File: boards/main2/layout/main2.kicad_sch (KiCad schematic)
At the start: 218 parts, among them IC1 STM32H725RGV6, IC2 LSM6DSVTR, IC6 STSPIN958TR, IC7 L6981C33DR, IC8 DRV8874PWPR, IC9 DRV8874PWPR, J1 B02B-PASK(LF)(SN), M1 B02B-PASK(LF)(SN), M2 B02B-PASK(LF)(SN), M3 B02B-PASK(LF)(SN), Q1 AO3400A, Q2 AO3400A, Q3 AO3400A, Q4 AO3400A, Q5 AO3400A, Q6 HSBB3072, Q8 AO3401A, Q9 AO3400A, SW1 DSHP04TJGER, SW2 GT-TC048B-H025-L1, SW3 GT-TC048B-H025-L1, SW4 MK-12D18-G040, SW5 GT-TC048B-H025-L1, U10 INA241A2IDGKR, U11 INA241A2IDGKR, U12 TLV9001IDBVR, U13 ESP32-S3-MINI-1-N8, U2 GT-USB-7010ASV, U6 USBLC6-2SC6, U8 ADP7142ACPZN3.3-R7, U9 INA228AIDGSR

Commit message: ✨ Give each main2 module its own schematic sheet
As on the main board: each module declares Project(..., layout=False), its signal ports take the
names of the nets they carry, GND_BAT is a ground port of REGULATORS, and erc.toml accepts the
two ERC warnings pcb 0.4.81's labels leave (diodeinc/pcb#1520). The netlist is unchanged (174
nets, same connectivity). The root's SENSORS pin labels run past the page's left edge until a pcb
release includes diodeinc/pcb#1522; tests/test_schematic.py expects it.
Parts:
- removed BZ1: FUET-5030, Team-Micras_MicrasPCB_components_fuet_FUET-5030:BUZ-SMD_FST-5030, symbol FUET-5030
- removed C100, C103, C106, C108, C18, C19, C20, C21, C24, C25, C32, C55, C59, C60, C70, C72, C79, C82, C88, C90, C91, C97: 100nF 10% 50V X7R, stdlib_kicad-footprints_Capacitor_SMD:C_0402_1005Metric, symbol C_Small
- removed C101, C104, C30: 10nF 10% 50V X7R, stdlib_kicad-footprints_Capacitor_SMD:C_0402_1005Metric, symbol C_Small
- removed C102, C105: 1nF 5% 50V C0G, stdlib_kicad-footprints_Capacitor_SMD:C_0402_1005Metric, symbol C_Small
- removed C107, C52, C63, C80, C81: 10uF 20% 25V X5R, stdlib_kicad-footprints_Capacitor_SMD:C_0603_1608Metric, symbol C_Small
- removed C109, C56, C57: 22uF 20% 25V X5R, stdlib_kicad-footprints_Capacitor_SMD:C_0805_2012Metric, symbol C_Small
- removed C110, C26, C27, C28, C29, C33, C53, C54, C69, C71: 1uF 10% 25V X5R, stdlib_kicad-footprints_Capacitor_SMD:C_0402_1005Metric, symbol C_Small
- removed C31: 220nF 10% 16V X7R, stdlib_kicad-footprints_Capacitor_SMD:C_0402_1005Metric, symbol C_Small
- removed C34, C35: 470nF 10% 50V X7R, stdlib_kicad-footprints_Capacitor_SMD:C_0603_1608Metric, symbol C_Small
- removed C36, C83, C84, C85, C86, C92, C93, C94, C95, C99: 10uF 10% 50V X7R, stdlib_kicad-footprints_Capacitor_SMD:C_1206_3216Metric, symbol C_Small
- removed C58: 47nF 10% 50V X7R, stdlib_kicad-footprints_Capacitor_SMD:C_0603_1608Metric, symbol C_Small
- removed C87, C96: 100uF 20% 25V, Team-Micras_MicrasPCB_components_jierr_JVS25V100M6X4:CAP-SMD_BD6.3-L6.6-W6.6-LS7.3-FD_JVS25V100M6X4, symbol JVS25V100M6X4
- removed C89, C98: 22nF 10% 50V X7R, stdlib_kicad-footprints_Capacitor_SMD:C_0402_1005Metric, symbol C_Small
- removed D1, D2: WS2812C-2020-V6, Team-Micras_MicrasPCB_components_worldsemi_WS2812C-2020:LED-SMD_4P-L2.2-W2.0-P1.00_WS2812C-2020-V6, symbol WS2812C-2020-V6
- removed D14: B5819W, Team-Micras_MicrasPCB_components_cj_B5819W:D_SOD-123, symbol B5819W
- removed D3: 1N4148W, Team-Micras_MicrasPCB_components_hongjiacheng_1N4148W:SOD-123_L2.7-W1.6-LS3.7-FD, symbol 1N4148W
- removed D4: LED YELLOW, stdlib_kicad-footprints_LED_SMD:LED_0603_1608Metric, symbol LED_Small_Filled_Yellow
- removed D5: LED RED, stdlib_kicad-footprints_LED_SMD:LED_0603_1608Metric, symbol LED_Small_Filled_Red
- removed D8: 5V TVS Diode, stdlib_kicad-footprints_Diode_SMD:D_SOD-882, symbol D_TVS_Small
- removed EC1, EC2: EncoderSlot, Team-Micras_MicrasPCB_components_micras_EncoderSlot:EncoderSlot_2x4_P0.95mm, symbol EncoderSlot
- removed ESP_BOOT1, ESP_EN1: TestPoint, Team-Micras_MicrasPCB_components_micras_TestPoint:TestPoint_Pad_D0.8mm, symbol TestPoint
- removed IC2: LSM6DSVTR, Team-Micras_MicrasPCB_components_st_LSM6DSV:LGA-14_3x2.5mm_P0.5mm, symbol LSM6DSV
- removed IC6: STSPIN958TR, Team-Micras_MicrasPCB_components_st_STSPIN958:QFN50P500X500X100-33N-D, symbol STSPIN958
- removed IC7: L6981C33DR, Team-Micras_MicrasPCB_components_st_L6981:SOIC127P600X175-8N, symbol L6981C33DR
- removed IC8, IC9: DRV8874PWPR, Team-Micras_MicrasPCB_components_ti_DRV8874:Texas_PWP0016J_HTSSOP-16-1EP_4.4x5mm_P0.65mm_EP3.4x5mm_Mask2.46x3.55mm, symbol DRV8874PWPR
- removed J1, M1, M2, M3: B02B-PASK(LF)(SN), Team-Micras_MicrasPCB_components_jst_B02B-PASK:JST_PA_B02B-PASK_1x02_P2.00mm_Vertical, symbol B02B-PASK
- removed L3: 22uH 20% 2.8A, Team-Micras_MicrasPCB_components_yjycoin_YSPIA0645-220M:IND-SMD_L6.5-W6.0, symbol YSPIA0645-220M
- removed L4, L5: 47uH 20% 4.1A, Team-Micras_MicrasPCB_components_coilcraft_XAL7070-473:L_Coilcraft_XAL7070-XXX, symbol XAL7070-473MEC
- removed L6: 4.7uH 20% 6.7A, Team-Micras_MicrasPCB_components_coilcraft_XGL5030-472:L_Coilcraft_XAL5030-XXX, symbol XGL5030-472MEC
- removed Q1, Q2, Q3, Q4, Q5, Q9: AO3400A, Team-Micras_MicrasPCB_components_aos_AO3400A:SOT-23-3_L2.9-W1.3-P1.90-LS2.4-BR, symbol AO3400A
- removed Q6: HSBB3072, Team-Micras_MicrasPCB_components_huashuo_HSBB3072:PRPAK-8_L3.0-W3.0-P0.65-BL-EP, symbol HSBB3072
- removed Q8: AO3401A, Team-Micras_MicrasPCB_components_aos_AO3401A:SOT-23, symbol AO3401A
- removed R1, R11, R15, R19, R23: 220 1%, stdlib_kicad-footprints_Resistor_SMD:R_0402_1005Metric, symbol R_Small
- removed R12, R16, R2, R20, R24, R42, R56, R60, R68, R69, R70, R80, R89, R90: 10k 1%, stdlib_kicad-footprints_Resistor_SMD:R_0402_1005Metric, symbol R_Small
- removed R13, R17, R21, R25: 3.3 1% 100mW, stdlib_kicad-footprints_Resistor_SMD:R_0603_1608Metric, symbol R_Small
- removed R14, R18, R22, R26, R30, R87: 1k 1%, stdlib_kicad-footprints_Resistor_SMD:R_0402_1005Metric, symbol R_Small
- removed R27: 39k 1%, stdlib_kicad-footprints_Resistor_SMD:R_0402_1005Metric, symbol R_Small
- removed R28, R91: 22k 1%, stdlib_kicad-footprints_Resistor_SMD:R_0402_1005Metric, symbol R_Small
- removed R29: 9.1k 1%, stdlib_kicad-footprints_Resistor_SMD:R_0402_1005Metric, symbol R_Small
- removed R3: 10 1% 250mW, stdlib_kicad-footprints_Resistor_SMD:R_1206_3216Metric, symbol R_Small
- removed R31: 25m 1% 1W, stdlib_kicad-footprints_Resistor_SMD:R_1206_3216Metric, symbol R_Small
- removed R4, R5, R81: 680 1%, stdlib_kicad-footprints_Resistor_SMD:R_0402_1005Metric, symbol R_Small
- removed R41, R43, R44, R49: 100k 1%, stdlib_kicad-footprints_Resistor_SMD:R_0402_1005Metric, symbol R_Small
- removed R45: 20k 1%, stdlib_kicad-footprints_Resistor_SMD:R_0402_1005Metric, symbol R_Small
- removed R47, R92: 33k 1%, stdlib_kicad-footprints_Resistor_SMD:R_0402_1005Metric, symbol R_Small
- removed R48: 82k 1%, stdlib_kicad-footprints_Resistor_SMD:R_0402_1005Metric, symbol R_Small
- removed R57: 1M 1%, stdlib_kicad-footprints_Resistor_SMD:R_0402_1005Metric, symbol R_Small
- removed R58, R84, R85, R86: 22 1%, stdlib_kicad-footprints_Resistor_SMD:R_0402_1005Metric, symbol R_Small
- removed R59: 2m 1% 1W, Team-Micras_MicrasPCB_components_vishay_WSK2512-MID:Vishay_WSK2512_6332Metric_1mR-4m9R, symbol WSK2512-MID
- removed R6, R7: 5.1k 1%, stdlib_kicad-footprints_Resistor_SMD:R_0402_1005Metric, symbol R_Small
- removed R61, R71: 2k 1%, stdlib_kicad-footprints_Resistor_SMD:R_0402_1005Metric, symbol R_Small
- removed R62, R72: 0, stdlib_kicad-footprints_Resistor_SMD:R_0402_1005Metric, symbol R_Small
- removed R63, R73: 5.6k 1%, stdlib_kicad-footprints_Resistor_SMD:R_0402_1005Metric, symbol R_Small
- removed R64, R74: 24k 1%, stdlib_kicad-footprints_Resistor_SMD:R_0402_1005Metric, symbol R_Small
- removed R65, R75: 10m 1% 1W, Team-Micras_MicrasPCB_components_vishay_WSK2512-HIGH:Vishay_WSK2512_6332Metric_5mR-200mR, symbol WSK2512-HIGH
- removed R66, R76, R77: 0 1W, stdlib_kicad-footprints_Resistor_SMD:R_2512_6332Metric, symbol R_Small
- removed R78, R79, R82, R88: 100 1%, stdlib_kicad-footprints_Resistor_SMD:R_0402_1005Metric, symbol R_Small
- removed R83: 1.2 0.1% 100mW, stdlib_kicad-footprints_Resistor_SMD:R_0603_1608Metric, symbol R_Small
- removed SW1: DSHP04TJGER, Team-Micras_MicrasPCB_components_kangshen_DSHP04TJGER:SW-SMD_8P-L6.7-W5.4-P1.27-LS5.6, symbol DSHP04TJGER
- removed SW2, SW3, SW5: GT-TC048B-H025-L1, Team-Micras_MicrasPCB_components_g-switch_GT-TC048B-H025-L1:SW-SMD-4P_L4.2-W3.2_GT-TC048, symbol GT-TC048B-H025-L1
- removed SW4: MK-12D18-G040, Team-Micras_MicrasPCB_components_g-switch_MK-12D18-G040:SW-TH_MK-12D18-G040, symbol MK-12D18-G040
- removed U10, U11: INA241A2IDGKR, Team-Micras_MicrasPCB_components_ti_INA241A2:Texas_DGK0008A_VSSOP-8_3x3mm_P0.65mm, symbol INA241A2
- removed U12: TLV9001IDBVR, Team-Micras_MicrasPCB_components_ti_TLV9001:SOT-23-5, symbol TLV9001IDBVR
- removed U13: ESP32-S3-MINI-1-N8, Team-Micras_MicrasPCB_components_espressif_ESP32-S3-MINI-1:ESP32-S3-MINI-1, symbol ESP32-S3-MINI-1
- removed U2: GT-USB-7010ASV, Team-Micras_MicrasPCB_components_g-switch_GT-USB-7010ASV:USB-C_G-Switch_GT-USB-7010ASV, symbol GT-USB-7010ASV
- removed U6: USBLC6-2SC6, Team-Micras_MicrasPCB_components_st_USBLC6-2SC6:SOT-23-6_ST_USBLC6-2SC6, symbol USBLC6-2SC6
- removed U8: ADP7142ACPZN3.3-R7, Team-Micras_MicrasPCB_components_adi_ADP7142:LFCSP-6-1EP_2x2mm_P0.65mm_EP1x1.6mm, symbol ADP7142ACPZN3.3-R7
- removed U9: INA228AIDGSR, Team-Micras_MicrasPCB_components_ti_INA228:Texas_DGS0010A_VSSOP-10_3x3mm_P0.5mm, symbol INA228
- removed W1, W2, W3, W4: WallSensor, Team-Micras_MicrasPCB_components_micras_WallSensor:WallSensor_SFH4550_TPS601A_THT, symbol WallSensor
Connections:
- no-connect marks 35 -> 0
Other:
- added sheet DRIVERS (DRIVERS.kicad_sch)
- added sheet ESP (ESP.kicad_sch)
- added sheet PERIPHERALS (PERIPHERALS.kicad_sch)
- added sheet REGULATORS (REGULATORS.kicad_sch)
- added sheet SENSORS (SENSORS.kicad_sch)
- moved on the sheet: C1, C10, C11, C12, C13, C14, C15, C16, C17, C2, C3, C4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

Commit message: 🐛 Keep main2's root labels on the page
SENSORS took three Spi ports, one per device, so the shared SCK, MISO and MOSI came in three times: 32 sheet pins. pcb 0.4.81 places the root's sheet symbols one by one in the order of their names, each as near the page centre as the earlier ones leave room and by its box alone, and a 32-pin SENSORS fitted only against the page's left edge, where the labels at its pins ran up to 11 mm past the page.

SENSORS now takes the bus once (SPI_SCK, SPI_MISO, SPI_MOSI) and each device's chip select (IMU_SPI_CSn, Encoder_Right_CSn, Encoder_Left_CSn), and builds the three Spi interfaces inside. With 26 pins it sits right of ESP, and every label is on its page, so the strict xfail in tests/test_schematic.py goes. The ports take their nets' names, which leaves 8 multiple_net_names warnings instead of 14. The netlist is unchanged: the same 174 nets with the same names and pins.
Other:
- sheet SENSORS ports: added Encoder_Left_CSn, Encoder_Right_CSn, IMU_SPI_CSn, SPI_MISO, SPI_MOSI, SPI_SCK; removed ENCODER_LEFT_SPI.CLK, ENCODER_LEFT_SPI.CS, ENCODER_LEFT_SPI.MISO, ENCODER_LEFT_SPI.MOSI, ENCODER_RIGHT_SPI.CLK, ENCODER_RIGHT_SPI.CS, ENCODER_RIGHT_SPI.MISO, ENCODER_RIGHT_SPI.MOSI, IMU_SPI.CLK, IMU_SPI.CS, IMU_SPI.MISO, IMU_SPI.MOSI
- moved on the sheet: C1, C10, C11, C12, C13, C14, C15, C16, C17, C2, C3, C4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

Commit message: 🎨 Place main2's root sheet: the MCU with its supply domains, and the module sheets
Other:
- note added: "M2 screw holes to the chassis"
- note added: "MCU: STM32H725RGV6, its supply domains and their decoupling"
- note added: "Module sheets: power, radio, user interface"
- note added: "Module sheets: sensors, drivers"
- note added: "Test pads: IMU interrupts and fan driver (bare pads)"
- note added: "Test pads: SWD backstop (bare pads)"
- title: (none) -> MCU and module sheets
- moved on the sheet: C1, C10, C11, C12, C13, C14, C15, C16, C17, C2, C3, C4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

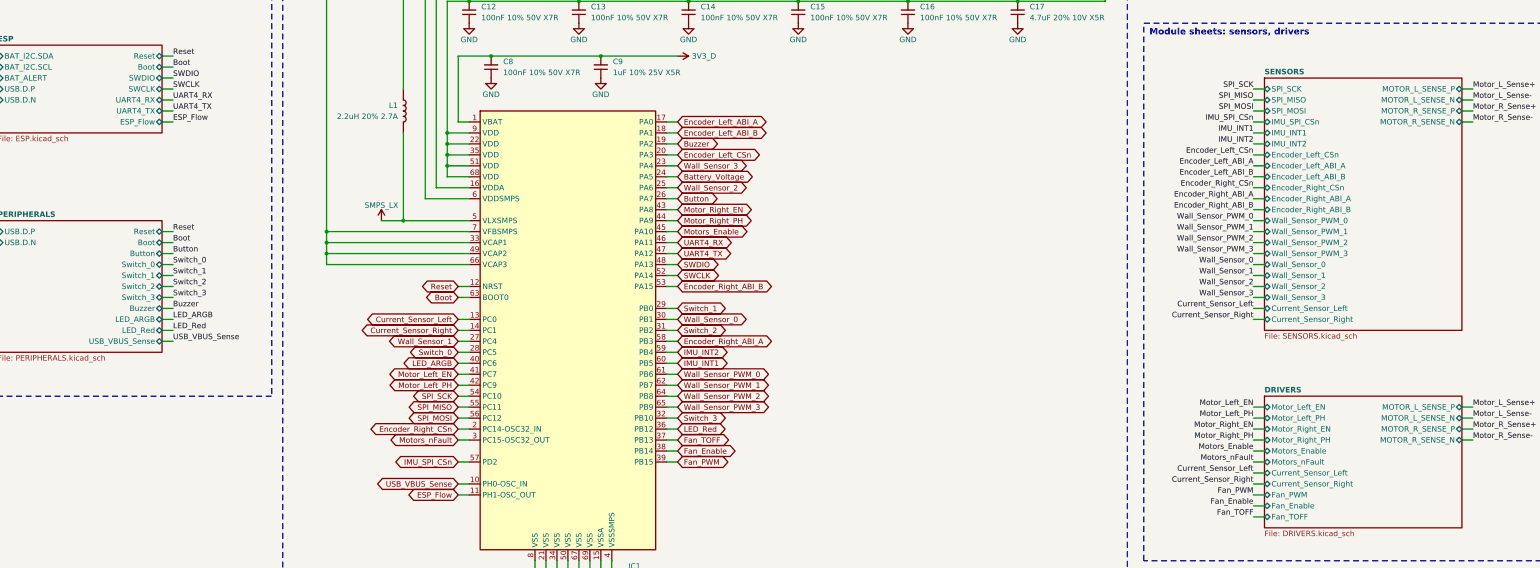
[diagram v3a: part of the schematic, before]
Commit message: ✨ Set main2's emitter current from the DAC and AC-couple its selectors
- The shared sink's set-point comes from PA5 (DAC1_OUT2, buffer off) through
  200k/20k, ratiometric to VDDA and 0 V at reset; 1k/1 nF compensates the loop
  into Q9 and 200k from 3V3_A turns the sink off at a zero set-point.
- Q2-Q5 keep the main board's AC-coupled gates (220 nF, 22k, 1N4148WS clamp):
  a pin held high turns its emitter off within 11 ms.
- Battery_Voltage moves to PC5, Switch_0 to PH0; the H7's VBUS divider goes,
  the ESP32 reports USB power over UART4.
- A test bench checks the selector coupling and the DAC set-point; the
  research model is calculations/emitter/emitter_sink.py.
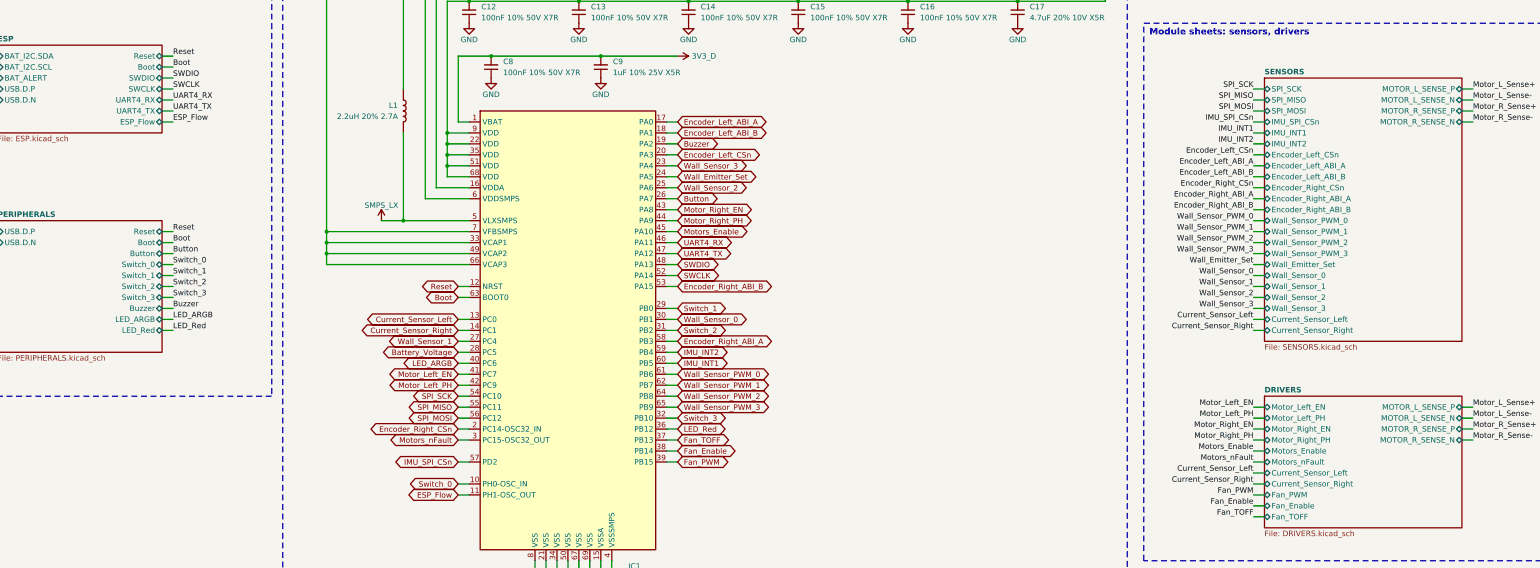
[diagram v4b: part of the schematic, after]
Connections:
- net USB_VBUS_Sense is gone; now on net Switch_0: IC1.10 (PH0-OSC_IN)
- net Battery_Voltage: now also IC1.28 (PC5); no longer IC1.24 (PA5)
- net Switch_0: no longer IC1.28 (PC5)
- new net Wall_Emitter_Set: IC1.24 (PA5)
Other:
- sheet PERIPHERALS ports: added none; removed USB_VBUS_Sense
- sheet SENSORS ports: added Wall_Emitter_Set; removed none
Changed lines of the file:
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@@
 			)
 		)
-		(pin "USB_VBUS_Sense" bidirectional
-			(at 83.82 144.78 0)
-			(effects
-				(font
-					(size 1.27 1.27)
-				)
-				(justify right)
-			)
-		)
 		(instances
 			(project "main2"
@@
 	(sheet
 		(at 339.09 83.82)
-		(size 45.72 58.42)
+		(size 45.72 60.96)
 		(exclude_from_sim no)
 		(in_bom yes)
@@
 		)
 		(property "Sheetfile" "SENSORS.kicad_sch"
-			(at 339.09 142.8338 0)
+			(at 339.09 145.3738 0)
 			(show_name no)
 			(do_not_autoplace no)
@@
 		)
 		(pin "Current_Sensor_Left" bidirectional
-			(at 339.09 137.16 180)
+			(at 339.09 139.7 180)
 			(effects
 				(font
@@
 		)
 		(pin "Current_Sensor_Right" bidirectional
-			(at 339.09 139.7 180)
+			(at 339.09 142.24 180)
 			(effects
 				(font
@@
 			)
 		)
-		(pin "Wall_Sensor_0" bidirectional
+		(pin "Wall_Emitter_Set" bidirectional
 			(at 339.09 127 180)
 			(effects
@@
 			)
 		)
-		(pin "Wall_Sensor_1" bidirectional
+		(pin "Wall_Sensor_0" bidirectional
 			(at 339.09 129.54 180)
 			(effects
@@
 			)
 		)
-		(pin "Wall_Sensor_2" bidirectional
+		(pin "Wall_Sensor_1" bidirectional
 			(at 339.09 132.08 180)
 			(effects
@@
 			)
 		)
-		(pin "Wall_Sensor_3" bidirectional
+		(pin "Wall_Sensor_2" bidirectional
 			(at 339.09 134.62 180)
 			(effects
@@
 			)
 		)
+		(pin "Wall_Sensor_3" bidirectional
+			(at 339.09 137.16 180)
+			(effects
+				(font
+					(size 1.27 1.27)
+				)
+				(justify left)
+			)
+		)
 		(pin "Wall_Sensor_PWM_0" bidirectional
 			(at 339.09 116.84 180)
@@
 	(wire
 		(pts
-			(xy 83.82 144.78) (xy 86.36 144.78)
-		)
-		(stroke
-			(width 0)
-			(type default)
-		)
-	)
-	(wire
-		(pts
 			(xy 45.72 53.34) (xy 43.18 53.34)
 		)
@@
 	(wire
 		(pts
-			(xy 339.09 137.16) (xy 336.55 137.16)
+			(xy 339.09 139.7) (xy 336.55 139.7)
 		)
 		(stroke
@@
 	(wire
 		(pts
-			(xy 339.09 139.7) (xy 336.55 139.7)
+			(xy 339.09 142.24) (xy 336.55 142.24)
 		)
 		(stroke
@@
 	(wire
 		(pts
+			(xy 339.09 137.16) (xy 336.55 137.16)
+		)
+		(stroke
+			(width 0)
+			(type default)
+		)
+	)
+	(wire
+		(pts
 			(xy 339.09 116.84) (xy 336.55 116.84)
 		)
@@
 		)
 	)
-	(global_label "USB_VBUS_Sense"
+	(global_label "Switch_0"
 		(shape bidirectional)
 		(at 152.4 177.8 180)
@@
 		)
 	)
-	(global_label "Battery_Voltage"
+	(global_label "Wall_Emitter_Set"
 		(shape bidirectional)
 		(at 203.2 106.68 0)
@@
 		)
 	)
-	(global_label "Switch_0"
+	(global_label "Battery_Voltage"
 		(shape bidirectional)
 		(at 152.4 147.32 180)
@@
 		)
 	)
-	(label "USB_VBUS_Sense"
-		(at 86.36 144.78 0)
-		(effects
-			(font
-				(size 1.27 1.27)
-			)
-			(justify left bottom)
-		)
-	)
 	(label "BAT_ALERT"
 		(at 43.18 53.34 180)
@@
 	)
 	(label "Current_Sensor_Left"
-		(at 336.55 137.16 180)
+		(at 336.55 139.7 180)
 		(effects
 			(font
@@
 	)
 	(label "Current_Sensor_Right"
-		(at 336.55 139.7 180)
+		(at 336.55 142.24 180)
 		(effects
 			(font
@@
 		)
 	)
-	(label "Wall_Sensor_0"
+	(label "Wall_Emitter_Set"
 		(at 336.55 127 180)
 		(effects
@@
 		)
 	)
-	(label "Wall_Sensor_1"
+	(label "Wall_Sensor_0"
 		(at 336.55 129.54 180)
 		(effects
@@
 		)
 	)
-	(label "Wall_Sensor_2"
+	(label "Wall_Sensor_1"
 		(at 336.55 132.08 180)
 		(effects
@@
 		)
 	)
-	(label "Wall_Sensor_3"
+	(label "Wall_Sensor_2"
 		(at 336.55 134.62 180)
 		(effects
 			(font
+				(size 1.27 1.27)
+			)
+			(justify right bottom)
+		)
+	)
+	(label "Wall_Sensor_3"
+		(at 336.55 137.16 180)
+		(effects
+			(font
